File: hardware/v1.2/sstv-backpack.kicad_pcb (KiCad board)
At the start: 2 copper layers, 38.1 x 63.5 mm, 29 parts, among them J1 Conn_01x03_Pin, J2 Conn_01x02_Pin, J4 USB_C_Receptacle_USB2.0_14P, Q1 MMBT3904, SW1 SW_Push, SW2 SLW-1276864-4A-D, U1 ESP32-CAM, U2 FT231XS

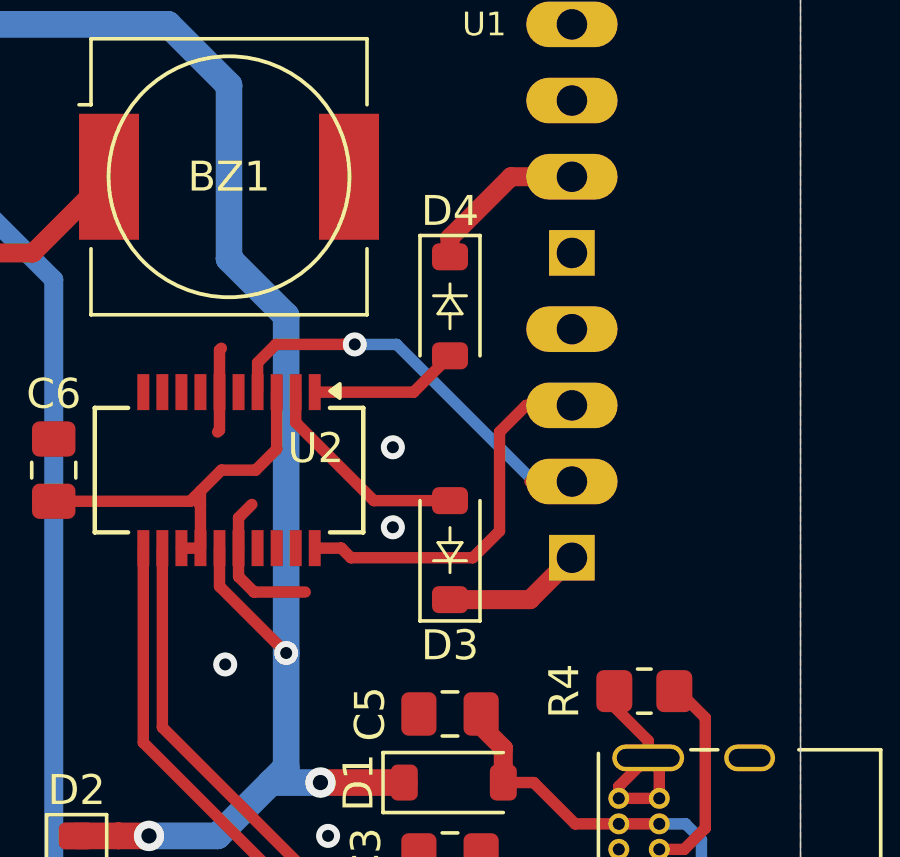
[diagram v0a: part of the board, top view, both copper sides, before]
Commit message: Update README and code for PTT
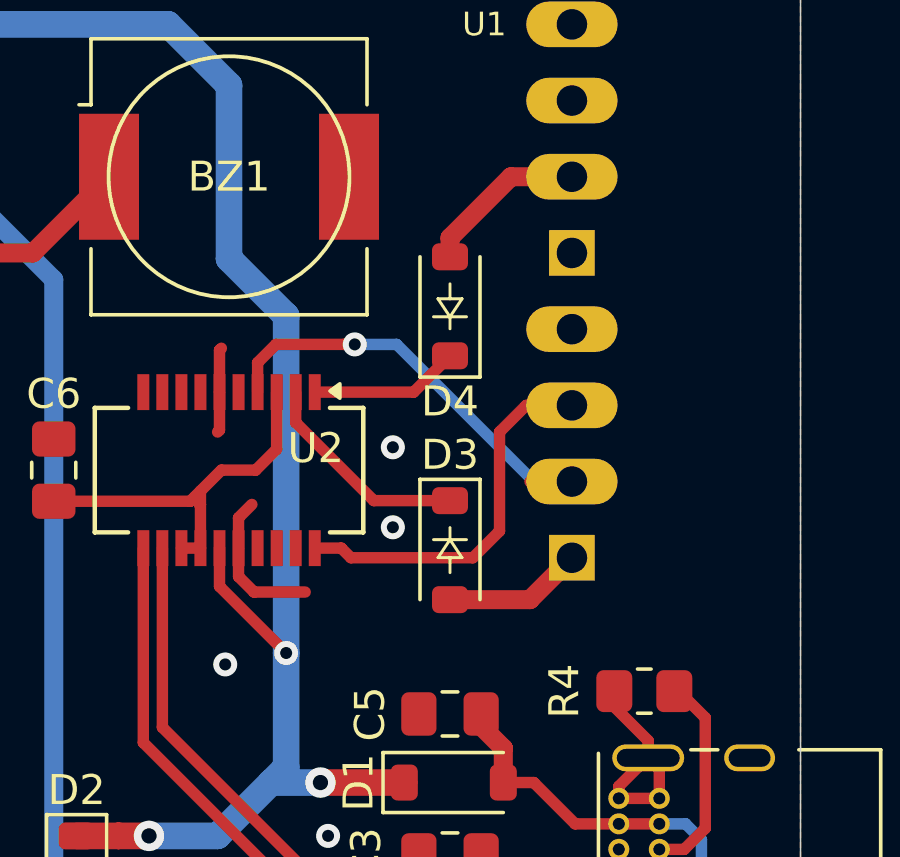
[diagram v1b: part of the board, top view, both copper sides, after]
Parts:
- R5: value 4.7k -> 10k
- turned D3 to -90 degrees
- turned D4 to 90 degrees
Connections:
- D3 pad 1: Net-(D3-K) -> RTS
- D3 pad 2: RTS -> Net-(D3-A)
- D4 pad 1: Net-(D4-K) -> DTR
- D4 pad 2: DTR -> Net-(D4-A)
- U1 pad P$1: Net-(D3-K) -> Net-(D3-A)
- U1 pad P$6: Net-(D4-K) -> Net-(D4-A)
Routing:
- net Net-(D4-K): track 5.54 -> 0.00 mm
- net Net-(D4-A): track 0.00 -> 5.54 mm
- net Net-(D3-K): track 4.64 -> 0.00 mm
- net Net-(D3-A): track 0.00 -> 4.64 mm
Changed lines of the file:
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@@
 	(net 36 "/CC1")
 	(net 37 "/5VO")
-	(net 38 "Net-(D3-K)")
-	(net 39 "Net-(D4-K)")
+	(net 38 "Net-(D3-A)")
+	(net 39 "Net-(D4-A)")
 	(footprint "Resistor_SMD:R_0805_2012Metric_Pad1.20x1.40mm_HandSolder"
 		(layer "F.Cu")
@@
 			)
 		)
-		(property "Value" "4.7k"
+		(property "Value" "10k"
 			(at 0 1.65 0)
 			(layer "F.Fab")
@@
 	(footprint "Diode_SMD:D_SOD-123"
 		(layer "F.Cu")
-		(at 166.116 87.376 90)
+		(at 166.116 87.376 -90)
 		(descr "SOD-123")
 		(tags "SOD-123")
@@
 		)
 		(property "Datasheet" ""
-			(at 0 0 90)
+			(at 0 0 270)
 			(unlocked yes)
 			(layer "F.Fab")
@@
 		)
 		(property "Description" "Diode"
-			(at 0 0 90)
+			(at 0 0 270)
 			(unlocked yes)
 			(layer "F.Fab")
@@
 		)
 		(property "Sim.Device" "D"
-			(at 0 0 90)
+			(at 0 0 270)
 			(unlocked yes)
 			(layer "F.Fab")
@@
 		)
 		(property "Sim.Pins" "1=K 2=A"
-			(at 0 0 90)
+			(at 0 0 270)
 			(unlocked yes)
 			(layer "F.Fab")
@@
 		(attr smd)
 		(fp_line
-			(start -2.36 -1)
-			(end 1.65 -1)
+			(start -2.36 1)
+			(end 1.65 1)
 			(stroke
 				(width 0.12)
@@
 		)
 		(fp_line
-			(start -2.36 -1)
-			(end -2.36 1)
+			(start 0.25 0.4)
+			(end -0.35 0)
 			(stroke
-				(width 0.12)
+				(width 0.1)
 				(type solid)
 			)
@@
 		)
 		(fp_line
-			(start 0.25 -0.4)
-			(end 0.25 0.4)
+			(start -0.75 0)
+			(end -0.35 0)
 			(stroke
 				(width 0.1)
@@
 		)
 		(fp_line
-			(start 0.25 0)
-			(end 0.75 0)
+			(start -0.35 0)
+			(end -0.35 0.55)
 			(stroke
 				(width 0.1)
@@
 		(fp_line
 			(start -0.35 0)
-			(end -0.35 -0.55)
+			(end 0.25 -0.4)
 			(stroke
 				(width 0.1)
@@
 		(fp_line
 			(start -0.35 0)
-			(end 0.25 -0.4)
+			(end -0.35 -0.55)
 			(stroke
 				(width 0.1)
@@
 		)
 		(fp_line
-			(start -0.35 0)
-			(end -0.35 0.55)
+			(start 0.25 0)
+			(end 0.75 0)
 			(stroke
 				(width 0.1)
@@
 		)
 		(fp_line
-			(start -0.75 0)
-			(end -0.35 0)
+			(start 0.25 -0.4)
+			(end 0.25 0.4)
 			(stroke
 				(width 0.1)
@@
 		)
 		(fp_line
-			(start 0.25 0.4)
-			(end -0.35 0)
+			(start -2.36 -1)
+			(end -2.36 1)
 			(stroke
-				(width 0.1)
+				(width 0.12)
 				(type solid)
 			)
@@
 		)
 		(fp_line
-			(start -2.36 1)
-			(end 1.65 1)
+			(start -2.36 -1)
+			(end 1.65 -1)
 			(stroke
 				(width 0.12)
@@
 		)
 		(fp_line
-			(start 2.35 -1.15)
-			(end 2.35 1.15)
+			(start 2.35 1.15)
+			(end -2.35 1.15)
 			(stroke
 				(width 0.05)
@@
 		(fp_line
 			(start -2.35 -1.15)
-			(end 2.35 -1.15)
+			(end -2.35 1.15)
 			(stroke
 				(width 0.05)
@@
 		(fp_line
 			(start -2.35 -1.15)
-			(end -2.35 1.15)
+			(end 2.35 -1.15)
 			(stroke
 				(width 0.05)
@@
 		)
 		(fp_line
-			(start 2.35 1.15)
-			(end -2.35 1.15)
+			(start 2.35 -1.15)
+			(end 2.35 1.15)
 			(stroke
 				(width 0.05)
@@
 		)
 		(fp_line
-			(start 1.4 -0.9)
-			(end 1.4 0.9)
+			(start -1.4 0.9)
+			(end -1.4 -0.9)
 			(stroke
 				(width 0.1)
@@
 		)
 		(fp_line
-			(start -1.4 -0.9)
-			(end 1.4 -0.9)
+			(start 1.4 0.9)
+			(end -1.4 0.9)
 			(stroke
 				(width 0.1)
@@
 		)
 		(fp_line
-			(start 1.4 0.9)
-			(end -1.4 0.9)
+			(start -1.4 -0.9)
+			(end 1.4 -0.9)
 			(stroke
 				(width 0.1)
@@
 		)
 		(fp_line
-			(start -1.4 0.9)
-			(end -1.4 -0.9)
+			(start 1.4 -0.9)
+			(end 1.4 0.9)
 			(stroke
 				(width 0.1)
@@
 		)
 		(pad "1" smd roundrect
-			(at -1.65 0 90)
+			(at -1.65 0 270)
 			(size 0.9 1.2)
 			(layers "F.Cu" "F.Mask" "F.Paste")
 			(roundrect_rratio 0.25)
-			(net 38 "Net-(D3-K)")
+			(net 1 "RTS")
 			(pinfunction "K")
 			(pintype "passive")
 		)
 		(pad "2" smd roundrect
-			(at 1.65 0 90)
+			(at 1.65 0 270)
 			(size 0.9 1.2)
 			(layers "F.Cu" "F.Mask" "F.Paste")
 			(roundrect_rratio 0.25)
-			(net 1 "RTS")
+			(net 38 "Net-(D3-A)")
 			(pinfunction "A")
 			(pintype "passive")
@@
 			(layers "*.Cu" "*.Mask")
 			(remove_unused_layers no)
-			(net 38 "Net-(D3-K)")
+			(net 38 "Net-(D3-A)")
 			(pinfunction "GND/R")
 			(pintype "bidirectional")
@@
 			(layers "*.Cu" "*.Mask")
 			(remove_unused_layers no)
-			(net 39 "Net-(D4-K)")
+			(net 39 "Net-(D4-A)")
 			(pinfunction "GPIO0")
 			(pintype "bidirectional")
@@
 	(footprint "Diode_SMD:D_SOD-123"
 		(layer "F.Cu")
-		(at 166.116 79.248 -90)
+		(at 166.116 79.248 90)
 		(descr "SOD-123")
 		(tags "SOD-123")
@@
 		)
 		(property "Datasheet" ""
-			(at 0 0 270)
+			(at 0 0 90)
 			(unlocked yes)
 			(layer "F.Fab")
@@
 		)
 		(property "Description" "Diode"
-			(at 0 0 270)
+			(at 0 0 90)
 			(unlocked yes)
 			(layer "F.Fab")
@@
 		)
 		(property "Sim.Device" "D"
-			(at 0 0 270)
+			(at 0 0 90)
 			(unlocked yes)
 			(layer "F.Fab")
@@
 		)
 		(property "Sim.Pins" "1=K 2=A"
-			(at 0 0 270)
+			(at 0 0 90)
 			(unlocked yes)
 			(layer "F.Fab")
@@
 		(attr smd)
 		(fp_line
-			(start -2.36 1)
-			(end 1.65 1)
+			(start -2.36 -1)
+			(end 1.65 -1)
 			(stroke
 				(width 0.12)
@@
 		)
 		(fp_line
-			(start 0.25 0.4)
-			(end -0.35 0)
+			(start -2.36 -1)
+			(end -2.36 1)
 			(stroke
-				(width 0.1)
+				(width 0.12)
 				(type solid)
 			)
@@
 		)
 		(fp_line
-			(start -0.75 0)
-			(end -0.35 0)
+			(start 0.25 -0.4)
+			(end 0.25 0.4)
 			(stroke
 				(width 0.1)
@@
 		)
 		(fp_line
-			(start -0.35 0)
-			(end -0.35 0.55)
+			(start 0.25 0)
+			(end 0.75 0)
 			(stroke
 				(width 0.1)
@@
 		(fp_line
 			(start -0.35 0)
-			(end 0.25 -0.4)
+			(end -0.35 -0.55)
 			(stroke
 				(width 0.1)
@@
 		(fp_line
 			(start -0.35 0)
-			(end -0.35 -0.55)
+			(end 0.25 -0.4)
 			(stroke
 				(width 0.1)
@@
 		)
 		(fp_line
-			(start 0.25 0)
-			(end 0.75 0)
+			(start -0.35 0)
+			(end -0.35 0.55)
 			(stroke
 				(width 0.1)
@@
 		)
 		(fp_line
-			(start 0.25 -0.4)
-			(end 0.25 0.4)
+			(start -0.75 0)
+			(end -0.35 0)
 			(stroke
 				(width 0.1)
@@
 		)
 		(fp_line
-			(start -2.36 -1)
-			(end -2.36 1)
+			(start 0.25 0.4)
+			(end -0.35 0)
 			(stroke
-				(width 0.12)
+				(width 0.1)
 				(type solid)
 			)
@@
 		)
 		(fp_line
-			(start -2.36 -1)
-			(end 1.65 -1)
+			(start -2.36 1)
+			(end 1.65 1)
 			(stroke
 				(width 0.12)
@@
 		)
 		(fp_line
-			(start 2.35 1.15)
-			(end -2.35 1.15)
+			(start 2.35 -1.15)
+			(end 2.35 1.15)
 			(stroke
 				(width 0.05)
@@
 		(fp_line
 			(start -2.35 -1.15)
-			(end -2.35 1.15)
+			(end 2.35 -1.15)
 			(stroke
 				(width 0.05)
@@
 		(fp_line
 			(start -2.35 -1.15)
-			(end 2.35 -1.15)
+			(end -2.35 1.15)
 			(stroke
 				(width 0.05)
@@
 		)
 		(fp_line
-			(start 2.35 -1.15)
-			(end 2.35 1.15)
+			(start 2.35 1.15)
+			(end -2.35 1.15)
 			(stroke
 				(width 0.05)
@@
 		)
 		(fp_line
-			(start -1.4 0.9)
-			(end -1.4 -0.9)
+			(start 1.4 -0.9)
+			(end 1.4 0.9)
 			(stroke
 				(width 0.1)
@@
 		)
 		(fp_line
-			(start 1.4 0.9)
-			(end -1.4 0.9)
+			(start -1.4 -0.9)
+			(end 1.4 -0.9)
 			(stroke
 				(width 0.1)
@@
 		)
 		(fp_line
-			(start -1.4 -0.9)
-			(end 1.4 -0.9)
+			(start 1.4 0.9)
+			(end -1.4 0.9)
 			(stroke
 				(width 0.1)
@@
 		)
 		(fp_line
-			(start 1.4 -0.9)
-			(end 1.4 0.9)
+			(start -1.4 0.9)
+			(end -1.4 -0.9)
 			(stroke
 				(width 0.1)
@@
 		)
 		(pad "1" smd roundrect
-			(at -1.65 0 270)
+			(at -1.65 0 90)
 			(size 0.9 1.2)
 			(layers "F.Cu" "F.Mask" "F.Paste")
 			(roundrect_rratio 0.25)
-			(net 39 "Net-(D4-K)")
+			(net 26 "DTR")
 			(pinfunction "K")
 			(pintype "passive")
 		)
 		(pad "2" smd roundrect
-			(at 1.65 0 270)
+			(at 1.65 0 90)
 			(size 0.9 1.2)
 			(layers "F.Cu" "F.Mask" "F.Paste")
 			(roundrect_rratio 0.25)
-			(net 26 "DTR")
+			(net 39 "Net-(D4-A)")
 			(pinfunction "A")
 			(pintype "passive")
